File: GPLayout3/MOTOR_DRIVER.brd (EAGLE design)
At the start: 91.4 x 97.5 mm, 91 parts, among them T1 2N2222, T2 2N2222, U7 ATMEGA328P_TQFP, Y1 16MHz

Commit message: Added component attributes
Added manufacturer, part number, and price to part attributes.
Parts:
- R1: value 2800 -> 2.8K
- R2: value 1620 -> 1.62K
- R3: value 2320 -> 2.32K
- R4: value 1150 -> 1.15K

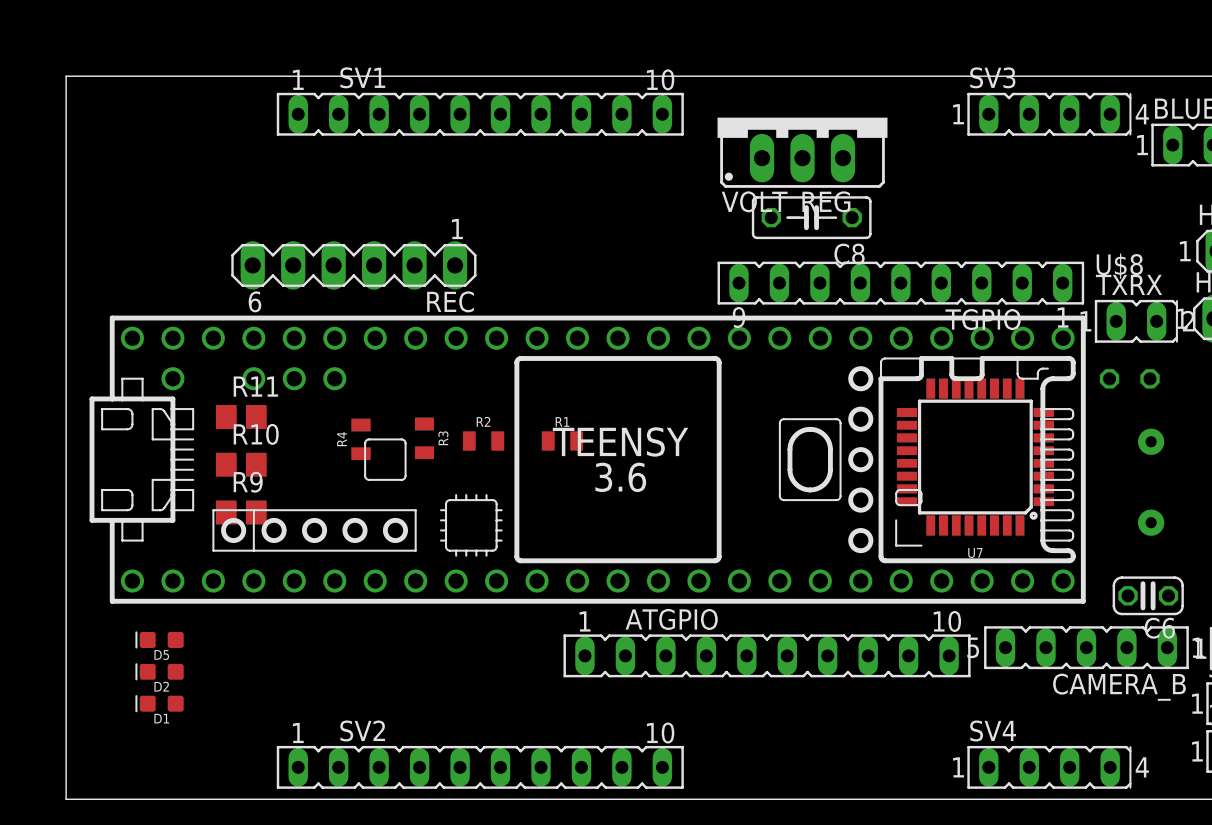
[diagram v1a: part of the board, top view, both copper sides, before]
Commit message: Fixed a couple top wires on gate driver chip and gnd
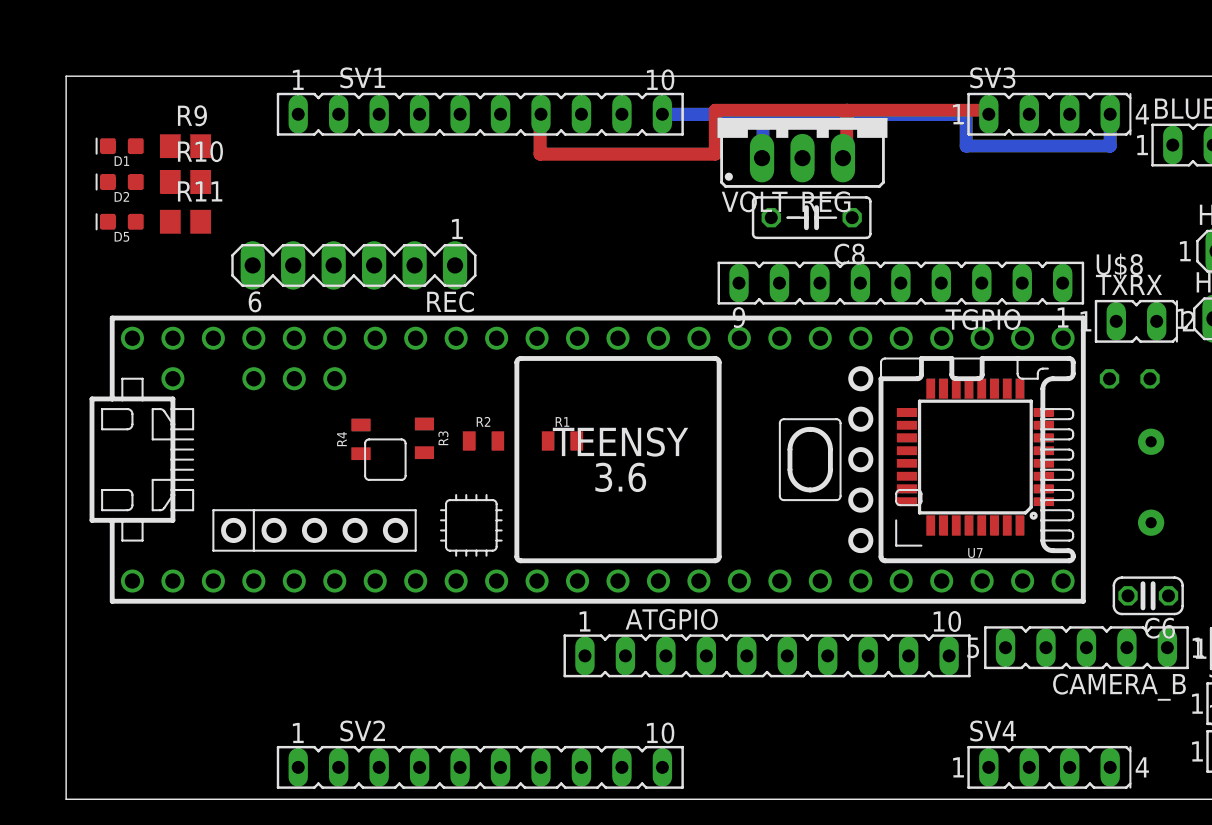
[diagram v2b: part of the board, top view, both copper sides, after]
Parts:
- moved D1 35.1 mm to (3.50, 41.0)
- moved D2 30.9 mm to (3.50, 38.8)
- moved D5 26.4 mm to (3.50, 36.2)
- moved R9 23.3 mm to (7.50, 41.0)
- moved R10 18.1 mm to (7.50, 38.8)
- moved R11 12.7 mm to (7.50, 36.2)
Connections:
- new net 7_V_LED: SV7.1
- new net GND_LED: SV7.4
- net 7_4V: now also SV3.1
- net GND: now also SV3.4
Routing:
- net 7_4V: track 0.00 -> 37.0 mm
- net GND: track 0.00 -> 34.9 mm
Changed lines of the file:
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@@
 <?xml version="1.0" encoding="utf-8"?>
 <!DOCTYPE eagle SYSTEM "eagle.dtd">
-<eagle version="8.0.1">
+<eagle version="8.0.0">
 <drawing>
 <settings>
@@
 <element name="3_3V" library="con-lsta" package="FE05-1" value="" x="78" y="3"/>
 <element name="5V" library="con-lsta" package="FE05-1" value="" x="78" y="6"/>
-<element name="R9" library="rcl" package="R0805" value="" x="11" y="18"/>
-<element name="R10" library="rcl" package="R0805" value="" x="11" y="21"/>
-<element name="R11" library="rcl" package="R0805" value="" x="11" y="24"/>
-<element name="D1" library="SparkFun-LED" package="LED-0603" value="" x="6" y="6" rot="R180"/>
-<element name="D2" library="SparkFun-LED" package="LED-0603" value="" x="6" y="8" rot="R180"/>
-<element name="D5" library="SparkFun-LED" package="LED-0603" value="" x="6" y="10" rot="R180"/>
+<element name="R9" library="rcl" package="R0805" value="" x="7.5" y="41"/>
+<element name="R10" library="rcl" package="R0805" value="" x="7.5" y="38.75"/>
+<element name="R11" library="rcl" package="R0805" value="" x="7.5" y="36.25"/>
+<element name="D1" library="SparkFun-LED" package="LED-0603" value="" x="3.5" y="41" rot="R180"/>
+<element name="D2" library="SparkFun-LED" package="LED-0603" value="" x="3.5" y="38.75" rot="R180"/>
+<element name="D5" library="SparkFun-LED" package="LED-0603" value="" x="3.5" y="36.25" rot="R180"/>
 <element name="TXRX" library="con-lsta" package="FE02-1" value="" x="71" y="30"/>
 <element name="LED1" library="Cree_XP" package="XP" value="CREE_XP" x="76" y="94"/>
@@
 <contactref element="D2" pad="C"/>
 <contactref element="D5" pad="C"/>
+<contactref element="SV3" pad="4"/>
+<wire x1="43.75" y1="43" x2="37.43" y2="43" width="0.8128" layer="16"/>
+<wire x1="43.75" y1="43" x2="56.5" y2="43" width="0.8128" layer="16"/>
+<wire x1="56.5" y1="43" x2="56.5" y2="41" width="0.8128" layer="16"/>
+<wire x1="56.5" y1="41" x2="65.54" y2="41" width="0.8128" layer="16"/>
+<wire x1="65.54" y1="41" x2="65.54" y2="43" width="0.8128" layer="16"/>
+<wire x1="43.686" y1="40.246" x2="43.75" y2="40.246" width="0.8128" layer="16"/>
+<wire x1="43.75" y1="40.246" x2="43.75" y2="43" width="0.8128" layer="16"/>
 <wire x1="83.126" y1="34.422" x2="85.698" y2="39.726" width="0" layer="19" extent="1-1"/>
 <wire x1="83.126" y1="30.082" x2="83.126" y2="34.422" width="0" layer="19" extent="1-1"/>
@@
 <wire x1="74.626" y1="30.162" x2="74.826" y2="34.402" width="0" layer="19" extent="1-1"/>
 <wire x1="74.55" y1="41.066" x2="74.826" y2="34.402" width="0" layer="19" extent="1-1"/>
+<wire x1="65.54" y1="41" x2="74.55" y2="41.066" width="0" layer="19" extent="16-16"/>
+<wire x1="44.264" y1="36.508" x2="43.686" y2="40.246" width="0" layer="19" extent="1-1"/>
+<wire x1="39.724" y1="28.938" x2="44.264" y2="36.508" width="0" layer="19" extent="1-1"/>
 <wire x1="65.5" y1="26.39" x2="74.626" y2="30.162" width="0" layer="19" extent="1-1"/>
 <wire x1="61.3706" y1="21.882" x2="65.5" y2="26.39" width="0" layer="19" extent="1-1"/>
@@
 <wire x1="69.13" y1="9.514" x2="66.66" y2="12.77" width="0" layer="19" extent="1-1"/>
 <wire x1="73.142" y1="9.45" x2="69.13" y2="9.514" width="0" layer="19" extent="1-1"/>
-<wire x1="39.724" y1="28.938" x2="52.7854" y2="21.082" width="0" layer="19" extent="1-1"/>
-<wire x1="44.264" y1="36.508" x2="39.724" y2="28.938" width="0" layer="19" extent="1-1"/>
-<wire x1="43.686" y1="40.246" x2="44.264" y2="36.508" width="0" layer="19" extent="1-1"/>
-<wire x1="37.43" y1="43" x2="43.686" y2="40.246" width="0" layer="19" extent="1-1"/>
 <wire x1="25.302" y1="22.49" x2="39.724" y2="28.938" width="0" layer="19" extent="1-1"/>
 <wire x1="24.414" y1="33.51" x2="25.302" y2="22.49" width="0" layer="19" extent="1-1"/>
 <wire x1="6.704" y1="28.938" x2="24.414" y2="33.51" width="0" layer="19" extent="1-1"/>
+<wire x1="2.623" y1="36.25" x2="6.704" y2="28.938" width="0" layer="19" extent="1-1"/>
+<wire x1="2.623" y1="38.75" x2="2.623" y2="36.25" width="0" layer="19" extent="1-1"/>
+<wire x1="2.623" y1="41" x2="2.623" y2="38.75" width="0" layer="19" extent="1-1"/>
 <wire x1="4.164" y1="13.698" x2="6.704" y2="28.938" width="0" layer="19" extent="1-1"/>
-<wire x1="5.123" y1="10" x2="4.164" y2="13.698" width="0" layer="19" extent="1-1"/>
-<wire x1="5.123" y1="8" x2="5.123" y2="10" width="0" layer="19" extent="1-1"/>
-<wire x1="5.123" y1="6" x2="5.123" y2="8" width="0" layer="19" extent="1-1"/>
 </signal>
 <signal name="N$6">
@@
 <contactref element="SV1" pad="7"/>
 <contactref element="R1" pad="2"/>
-<wire x1="29.81" y1="43" x2="48.766" y2="40.246" width="0" layer="19" extent="1-1"/>
-<wire x1="32.058" y1="22.49" x2="29.81" y2="43" width="0" layer="19" extent="1-1"/>
+<contactref element="SV3" pad="1"/>
+<wire x1="29.81" y1="43" x2="29.75" y2="43" width="0.8128" layer="1"/>
+<wire x1="29.75" y1="43" x2="29.75" y2="40.5" width="0.8128" layer="1"/>
+<wire x1="29.75" y1="40.5" x2="40.75" y2="40.5" width="0.8128" layer="1"/>
+<wire x1="40.75" y1="40.5" x2="40.75" y2="43.25" width="0.8128" layer="1"/>
+<wire x1="49" y1="43.25" x2="40.75" y2="43.25" width="0.8128" layer="1"/>
+<wire x1="49" y1="43.25" x2="57.92" y2="43.25" width="0.8128" layer="1"/>
+<wire x1="57.92" y1="43.25" x2="57.92" y2="43" width="0.8128" layer="1"/>
+<wire x1="48.766" y1="40.246" x2="49" y2="40.246" width="0.8128" layer="1"/>
+<wire x1="49" y1="40.246" x2="49" y2="43.25" width="0.8128" layer="1"/>
+<wire x1="32.058" y1="22.49" x2="29.75" y2="40.5" width="0" layer="19" extent="1-1"/>
 </signal>
 <signal name="BATT_VOLTAGE">
@@
 <contactref element="U$1" pad="14/A0"/>
 <contactref element="R9" pad="2"/>
-<wire x1="11.95" y1="18" x2="34.644" y2="28.938" width="0" layer="19" extent="1-1"/>
+<wire x1="8.45" y1="41" x2="34.644" y2="28.938" width="0" layer="19" extent="1-1"/>
 </signal>
 <signal name="LED2">
 <contactref element="U$1" pad="15/A1"/>
 <contactref element="R10" pad="2"/>
-<wire x1="11.95" y1="21" x2="32.104" y2="28.938" width="0" layer="19" extent="1-1"/>
+<wire x1="8.45" y1="38.75" x2="32.104" y2="28.938" width="0" layer="19" extent="1-1"/>
 </signal>
 <signal name="LED3">
 <contactref element="U$1" pad="16/A2"/>
 <contactref element="R11" pad="2"/>
-<wire x1="11.95" y1="24" x2="29.564" y2="28.938" width="0" layer="19" extent="1-1"/>
+<wire x1="8.45" y1="36.25" x2="29.564" y2="28.938" width="0" layer="19" extent="1-1"/>
 </signal>
 <signal name="N$1">
@@
 <contactref element="R9" pad="1"/>
 <contactref element="D1" pad="A"/>
-<wire x1="6.877" y1="6" x2="10.05" y2="18" width="0" layer="19" extent="1-1"/>
+<wire x1="4.377" y1="41" x2="6.55" y2="41" width="0" layer="19" extent="1-1"/>
 </signal>
 <signal name="N$23">
 <contactref element="R10" pad="1"/>
 <contactref element="D2" pad="A"/>
-<wire x1="6.877" y1="8" x2="10.05" y2="21" width="0" layer="19" extent="1-1"/>
+<wire x1="4.377" y1="38.75" x2="6.55" y2="38.75" width="0" layer="19" extent="1-1"/>
 </signal>
 <signal name="N$24">
 <contactref element="R11" pad="1"/>
 <contactref element="D5" pad="A"/>
-<wire x1="6.877" y1="10" x2="10.05" y2="24" width="0" layer="19" extent="1-1"/>
+<wire x1="4.377" y1="36.25" x2="6.55" y2="36.25" width="0" layer="19" extent="1-1"/>
 </signal>
 <signal name="LED1HI">
@@
 <wire x1="14.57" y1="2" x2="16.864" y2="13.698" width="0" layer="19" extent="1-1"/>
 </signal>
+<signal name="7_V_LED">
+<contactref element="SV7" pad="1"/>
+</signal>
+<signal name="GND_LED">
+<contactref element="SV7" pad="4"/>
+</signal>
 </signals>

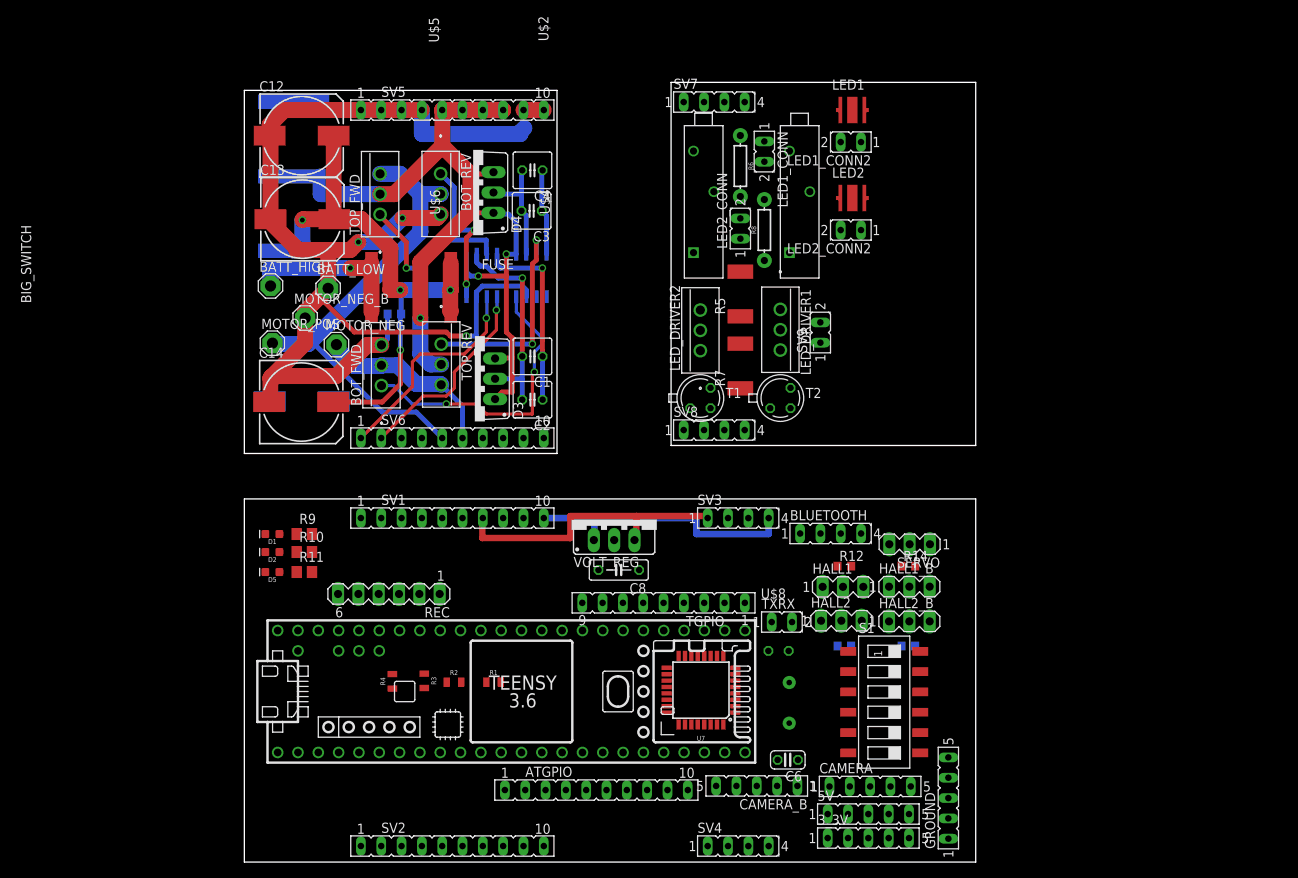
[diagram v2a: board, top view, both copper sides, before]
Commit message: Added more wires to top board
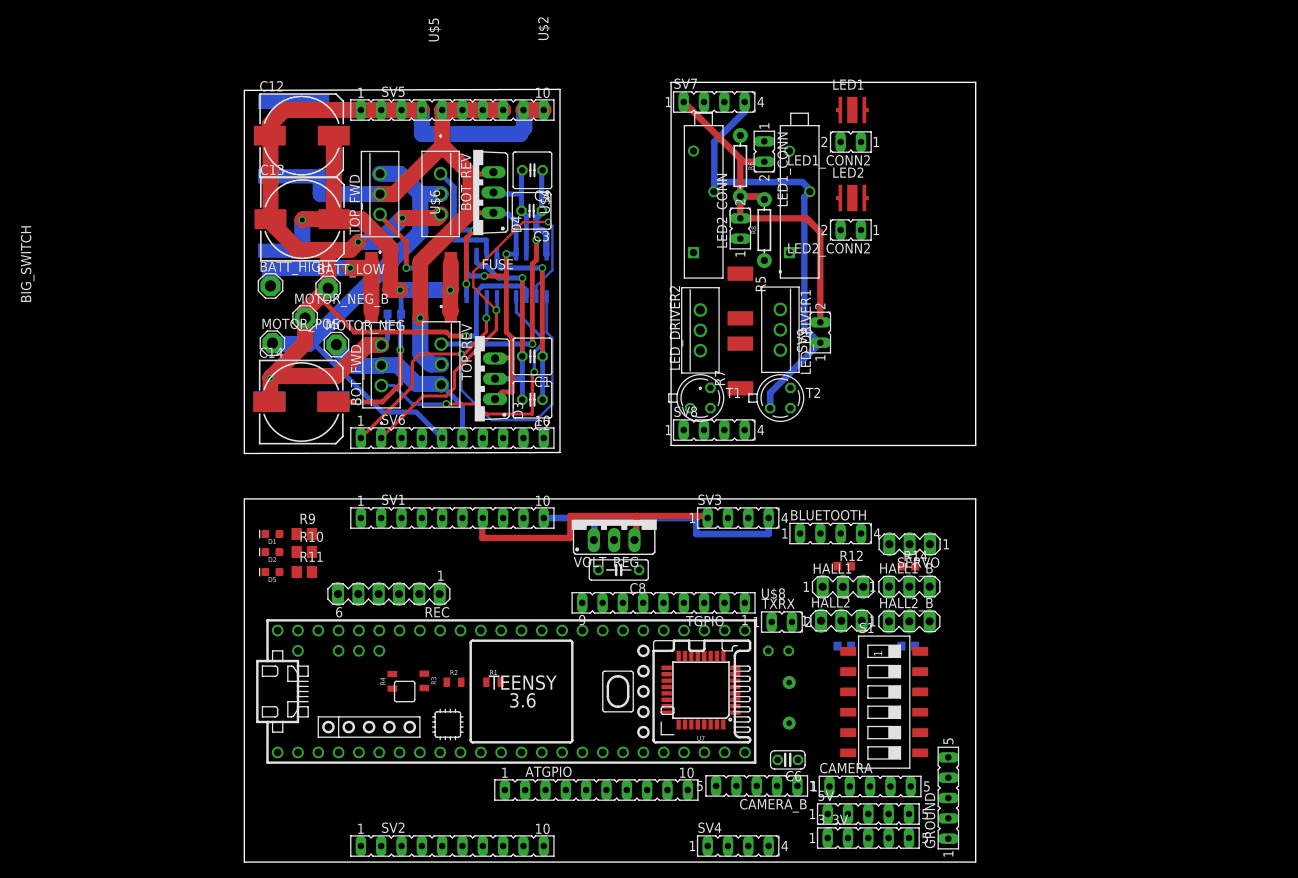
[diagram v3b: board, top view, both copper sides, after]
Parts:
- moved R5 0.25 mm to (62.0, 70.8), turned to 270 degrees
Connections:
- removed net 7_V_LED: SV7.1
- removed net GND_LED: SV7.4
- net 7_4V_TOP2: now also SV7.1
- net GND_TOP2: now also SV7.4
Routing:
- net GND_TOP2: track 0.00 -> 56.3 mm
- net 7_4V_TOP2: track 0.00 -> 45.7 mm
- net LI_TOP: track 27.4 -> 59.4 mm, vias 1 -> 2
- net HI_TOP: track 25.4 -> 53.6 mm, vias 1 -> 2
- net GND_TOP: track 155.1 -> 160.3 mm, vias 3 -> 4
- net N$21: track 67.3 -> 70.4 mm, vias 4 -> 5
- net N$11: track 10.8 -> 11.8 mm
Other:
- outline, holes or cut-outs redrawn

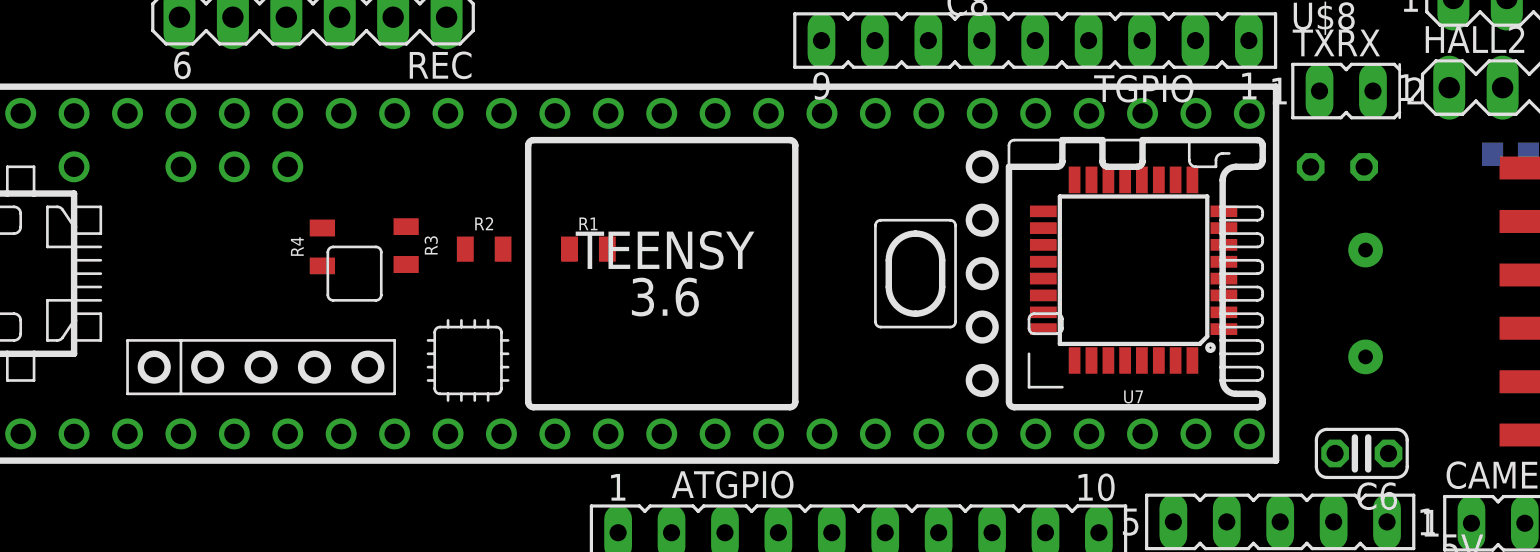
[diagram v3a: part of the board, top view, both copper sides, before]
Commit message: Fixed silkscreen for bottom layer
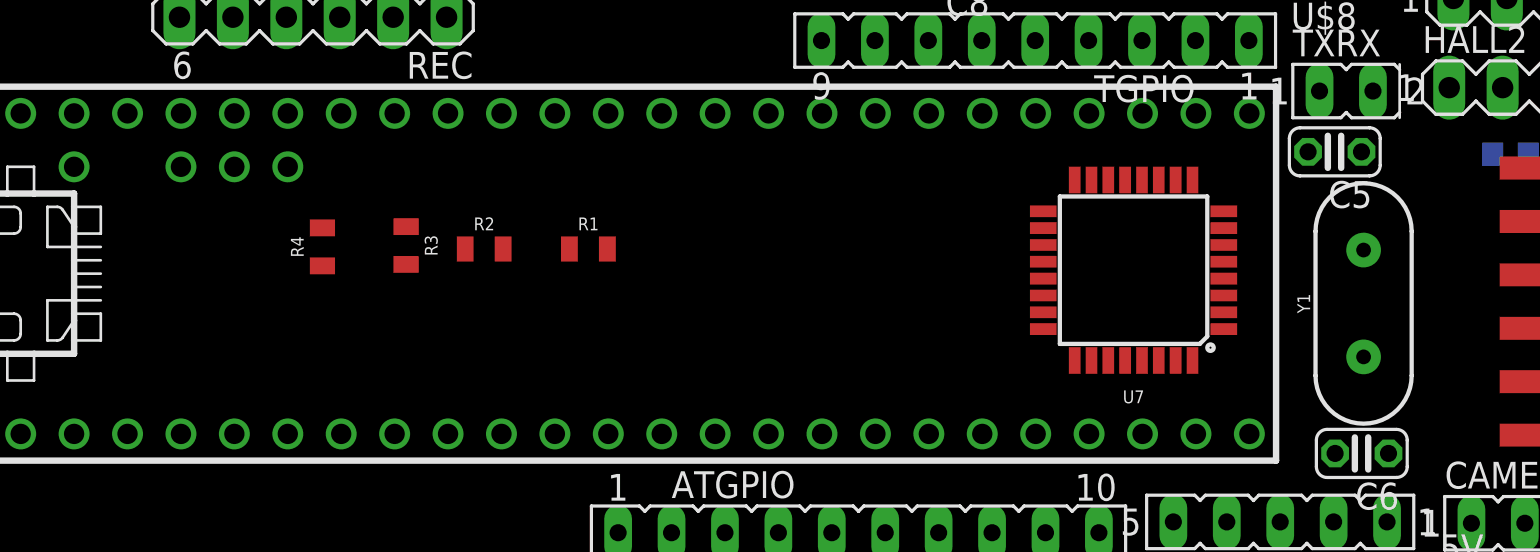
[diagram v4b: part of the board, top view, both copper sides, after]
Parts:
- moved C5 0.73 mm to (66.6, 27.1), flipped to the top, turned to 180 degrees
- moved Y1 0.09 mm to (68.0, 19.9), flipped to the top
